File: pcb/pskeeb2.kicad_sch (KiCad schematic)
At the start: 29 parts, among them J1 OLED, K11 KEYSW, K12 KEYSW, K13 KEYSW, K14 KEYSW, K15 KEYSW, K21 KEYSW, K22 KEYSW, K23 KEYSW, K24 KEYSW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

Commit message: feat: finish design
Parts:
- removed J1: OLED, Connector_PinHeader_2.54mm:PinHeader_1x04_P2.54mm_Vertical, symbol Connector:Conn_01x04_Male
- removed U1: wemos-esp32-s2-mini, kwkb-footprint:WEMOS_S2_mini, symbol kwkb:wemos-esp32-s2-mini
- added U1: YAAJ_WeAct_BlackPill_Part_Like, WeAct_BlackPill:YAAJ_WeAct_BlackPill_2, symbol YAAJ_WeAct_BlackPill_Part_Like:YAAJ_WeAct_BlackPill_Part_Like
- added U5: PlaceHoler, kwkb-footprint:T400-Trackpoint, symbol kwkb:PlaceHoler
- K11, K12, K13, K14, K15, K21, K22, K23, K24, K25, K31, K32, K33, K34, K35, K41, K42, K43: footprint kwkb-footprint:Gateron Choc Reversible -> kwkb-footprint:Mx-Choc-Reversible
- SW1, SW2: footprint Rotary_Encoder:RotaryEncoder_Alps_EC11E-Switch_Vertical_H20mm -> Keebio-Parts:RotaryEncoder_EC11-no-legs
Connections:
- net +3V3: now also U2.1 (SLEEVE), U3.1 (SLEEVE), U1.20 (3V3); no longer U2. (TIP), U3. (TIP)
- net +5V: now also U1.18 (5V)
- net ENA: now also U1.23 (PC14)
- net ENB: now also U1.24 (PC15)
- net GND: now also U2.4 (TIP), U3.4 (TIP), U1.19 (GND); no longer U2. (TIP), U3. (TIP)
- net RX: now also U2.2 (RING2), U3.3 (RING1), U1.15 (PB7); no longer U2. (TIP), U3. (TIP)
- net TX: now also U2.3 (RING1), U3.2 (RING2), U1.14 (PB6); no longer U2. (TIP), U3. (TIP)
- net k11: now also U1.1 (PB12)
- net k12: now also U1.4 (PB15)
- net k13: now also U1.37 (PB10)
- net k14: now also U1.35 (PB1)
- net k15: now also U1.34 (PB0)
- net k21: now also U1.2 (PB13)
- net k22: now also U1.5 (PA8)
- net k23: now also U1.16 (PB8)
- net k24: now also U1.30 (PA4)
- net k25: now also U1.29 (PA3)
- net k31: now also U1.3 (PB14)
- net k32: now also U1.10 (PA15)
- net k33: now also U1.17 (PB9)
- net k34: now also U1.27 (PA1)
- net k35: now also U1.28 (PA2)
- net k41: now also U1.11 (PB3)
- net k42: now also U1.12 (PB4)
- net k43: now also U1.13 (PB5)
- net k44: now also U1.26 (PA0)
- no-connect marks 0 -> 11
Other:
- note added: "Blackpill"
- note added: "TRACKPOINT CIRCUIT"
- note added: "TRRS JACK"
- moved on the sheet: C1, R1, R2, R3, U4

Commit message: feat: shipped to factory  for the pilot
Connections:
- net TP_CLK: now also U1.33 (PA7)
- net TP_DAT: now also U1.32 (PA6)
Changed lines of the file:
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@@
+    )
+  )
+  (global_label "TP_CLK" (shape input) (at 82.55 64.77 0) (fields_autoplaced)
+    (effects (font (size 1.27 1.27)) (justify left))
+    (property "Intersheet References" "${INTERSHEET_REFS}" (id 0) (at 91.7364 64.8494 0)
+      (effects (font (size 1.27 1.27)) (justify left) hide)
     )
   )
@@
       (effects (font (size 1.27 1.27)) (justify left) hide)
     )
+  )
+  (global_label "TP_DAT" (shape input) (at 82.55 67.31 0) (fields_autoplaced)
+    (effects (font (size 1.27 1.27)) (justify left))
+    (property "Intersheet References" "${INTERSHEET_REFS}" (id 0) (at 91.4945 67.3894 0)
+      (effects (font (size 1.27 1.27)) (justify left) hide)
+    )

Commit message: fix: switch courtyard too small / trackpoint mounting
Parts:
- U4: footprint Connector_PinHeader_2.54mm:PinHeader_1x05_P2.54mm_Vertical_SMD_Pin1Left -> kwkb-footprint:HY20_1x05_P2.00mm_Vertical_SMD
- U5: footprint kwkb-footprint:T400-Trackpoint -> kwkb-footprint:T400-Trackpoint-mix
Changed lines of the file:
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@@
       (effects (font (size 1.27 1.27)) (justify left))
     )
-    (property "Footprint" "Connector_PinHeader_2.54mm:PinHeader_1x05_P2.54mm_Vertical_SMD_Pin1Left" (id 2) (at 135.89 165.1 0)
+    (property "Footprint" "kwkb-footprint:HY20_1x05_P2.00mm_Vertical_SMD" (id 2) (at 135.89 165.1 0)
       (effects (font (size 1.27 1.27)) hide)
     )
@@
       (effects (font (size 1.27 1.27)) (justify left))
     )
-    (property "Footprint" "kwkb-footprint:T400-Trackpoint" (id 2) (at 154.94 189.23 0)
+    (property "Footprint" "kwkb-footprint:T400-Trackpoint-mix" (id 2) (at 154.94 189.23 0)
       (effects (font (size 1.27 1.27)) hide)
     )
@@
     )
     (path "/a806eb4a-36cd-4061-851e-a8c4a8590c5a"
-      (reference "U4") (unit 1) (value "trackpoint") (footprint "Connector_PinHeader_2.54mm:PinHeader_1x05_P2.54mm_Vertical_SMD_Pin1Left")
+      (reference "U4") (unit 1) (value "trackpoint") (footprint "kwkb-footprint:HY20_1x05_P2.00mm_Vertical_SMD")
     )
     (path "/d9f85360-d33c-4d0c-a003-87975601c18b"
-      (reference "U5") (unit 1) (value "PlaceHoler") (footprint "kwkb-footprint:T400-Trackpoint")
-    )
-  )
+      (reference "U5") (unit 1) (value "PlaceHoler") (footprint "kwkb-footprint:T400-Trackpoint-mix")
+    )
+  )

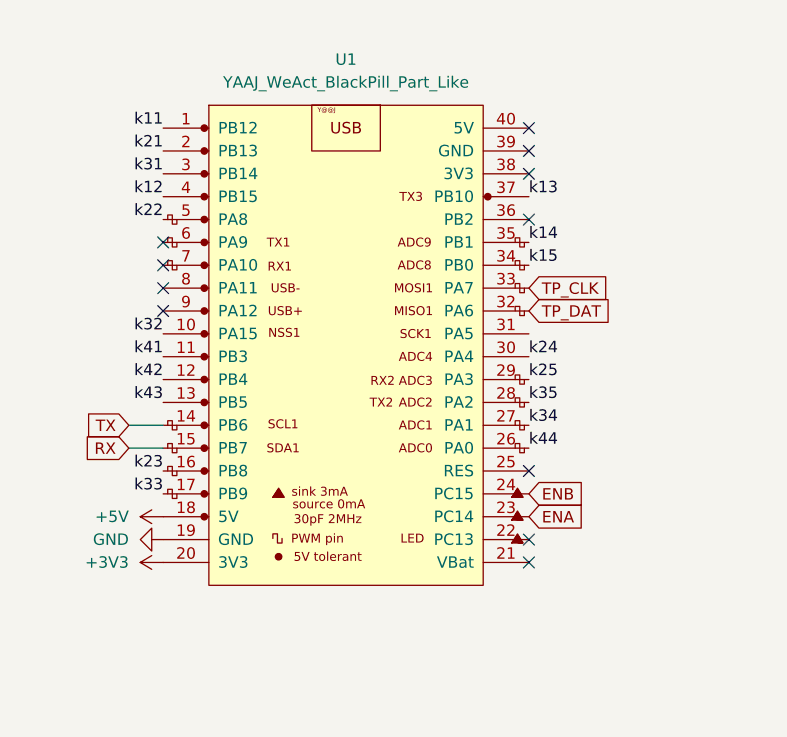
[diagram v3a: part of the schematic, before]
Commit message: fix: leave more space for soldering / use gh1.25 socket for trackpoint
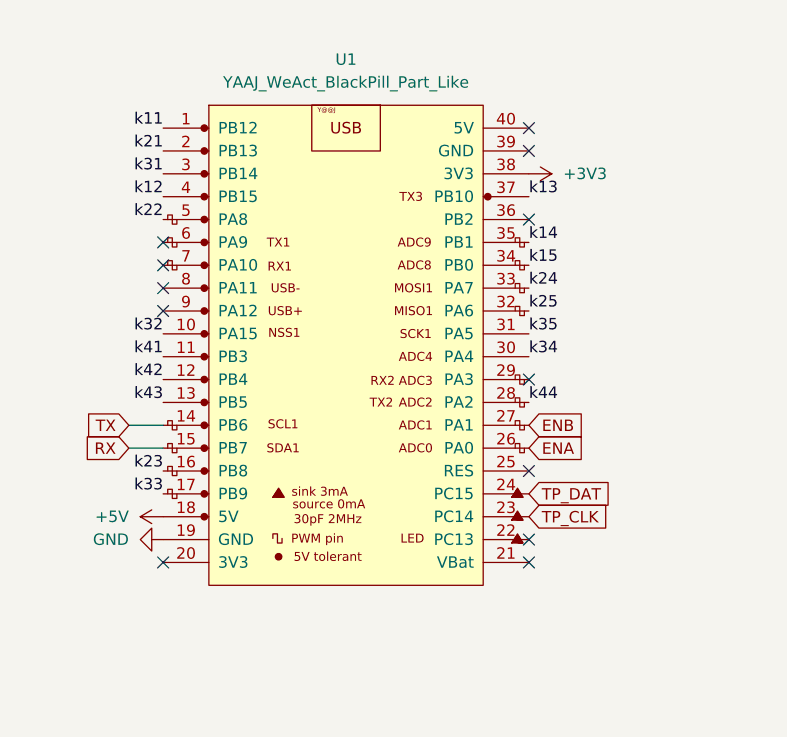
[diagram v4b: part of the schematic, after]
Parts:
- K11, K12, K13, K14, K15, K21, K22, K23, K24, K25, K31, K32, K33, K34, K35, K41, K42, K43: footprint kwkb-footprint:Mx-Choc-Reversible -> kwkb-footprint:Mx-Choc-Rev
- U4: footprint kwkb-footprint:HY20_1x05_P2.00mm_Vertical_SMD -> Connector_JST:JST_GH_SM05B-GHS-TB_1x05-1MP_P1.25mm_Horizontal
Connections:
- net +3V3: now also U1.38 (3V3); no longer U1.20 (3V3)
- net ENA: now also U1.26 (PA0); no longer U1.23 (PC14)
- net ENB: now also U1.27 (PA1); no longer U1.24 (PC15)
- net TP_CLK: now also U1.23 (PC14); no longer U1.33 (PA7)
- net TP_DAT: now also U1.24 (PC15); no longer U1.32 (PA6)
- net k24: now also U1.33 (PA7); no longer U1.30 (PA4)
- net k25: now also U1.32 (PA6); no longer U1.29 (PA3)
- net k34: now also U1.30 (PA4); no longer U1.27 (PA1)
- net k35: now also U1.31 (PA5); no longer U1.28 (PA2)
- net k44: now also U1.28 (PA2); no longer U1.26 (PA0)
- no-connect marks 11 -> 12

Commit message: chore: rev 2.4
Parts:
- SW1, SW2: footprint Keebio-Parts:RotaryEncoder_EC11-no-legs -> kwkb-footprint:RotaryEncoder_EC11-no-legs
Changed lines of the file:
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@@
     (property "Reference" "SW1" (id 0) (at 210.82 127 0))
     (property "Value" "RotaryEncoder_Switch" (id 1) (at 210.82 129.54 0))
-    (property "Footprint" "Keebio-Parts:RotaryEncoder_EC11-no-legs" (id 2) (at 207.01 133.096 0)
+    (property "Footprint" "kwkb-footprint:RotaryEncoder_EC11-no-legs" (id 2) (at 207.01 133.096 0)
       (effects (font (size 1.27 1.27)) hide)
     )
@@
     (property "Reference" "SW2" (id 0) (at 248.92 127 0))
     (property "Value" "RotaryEncoder_Switch" (id 1) (at 248.92 129.54 0))
-    (property "Footprint" "Keebio-Parts:RotaryEncoder_EC11-no-legs" (id 2) (at 245.11 133.096 0)
+    (property "Footprint" "kwkb-footprint:RotaryEncoder_EC11-no-legs" (id 2) (at 245.11 133.096 0)
       (effects (font (size 1.27 1.27)) hide)
     )
@@
     )
     (path "/1d095d65-ab42-481a-a9ed-ba71aa2d59a8"
-      (reference "SW1") (unit 1) (value "RotaryEncoder_Switch") (footprint "Keebio-Parts:RotaryEncoder_EC11-no-legs")
+      (reference "SW1") (unit 1) (value "RotaryEncoder_Switch") (footprint "kwkb-footprint:RotaryEncoder_EC11-no-legs")
     )
     (path "/3a6c8f40-fd54-4cfb-af3a-88db1915ff51"
-      (reference "SW2") (unit 1) (value "RotaryEncoder_Switch") (footprint "Keebio-Parts:RotaryEncoder_EC11-no-legs")
+      (reference "SW2") (unit 1) (value "RotaryEncoder_Switch") (footprint "kwkb-footprint:RotaryEncoder_EC11-no-legs")
     )
     (path "/af2183fb-a949-4f1f-8eb1-6ee101455a80"
